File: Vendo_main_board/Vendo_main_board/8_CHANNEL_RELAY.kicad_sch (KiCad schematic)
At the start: 75 parts, among them J10 Conn_01x03_Pin, J11 Conn_01x03_Pin, J12 Conn_01x03_Pin, J5 Conn_01x03_Pin, J6 Conn_01x03_Pin, J7 Conn_01x03_Pin, J8 Conn_01x03_Pin, J9 Conn_01x03_Pin, K1 SRD-05VDC-SL-C, K2 SRD-05VDC-SL-C, K3 SRD-05VDC-SL-C, K4 SRD-05VDC-SL-C, K5 SRD-05VDC-SL-C, K6 SRD-05VDC-SL-C, K7 SRD-05VDC-SL-C, K8 SRD-05VDC-SL-C, Q1 Q_NMOS_Depletion_GSD, Q2 Q_NMOS_Depletion_GSD, Q3 Q_NMOS_Depletion_GSD, Q4 Q_NMOS_Depletion_GSD, Q5 Q_NMOS_Depletion_GSD, Q6 Q_NMOS_Depletion_GSD, Q7 Q_NMOS_Depletion_GSD, Q8 Q_NMOS_Depletion_GSD, U10 PC817, U11 74HC595, U13 PC817, U14 PC817, U15 PC817, U16 PC817, U7 PC817, U8 PC817, U9 PC817

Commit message: -
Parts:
- added J13, J30, J31, J32, J33, J34, J35, J36: Conn_01x02_Pin, symbol Connector:Conn_01x02_Pin
- added J22, J23, J24, J25, J26, J27, J28, J29: Conn_01x03_Pin, symbol Connector:Conn_01x03_Pin
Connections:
- net DC_IN_1_A: now also J13.1 (Pin_1)
- net DC_IN_2_A: now also J30.1 (Pin_1)
- net DC_IN_3_A: now also J31.1 (Pin_1)
- net DC_IN_4_B: now also J32.1 (Pin_1)
- net DC_IN_5_A: now also J36.1 (Pin_1)
- net DC_IN_6_A: now also J35.1 (Pin_1)
- net DC_IN_7_A: now also J34.1 (Pin_1)
- net DC_IN_8_A: now also J33.1 (Pin_1)
- net GNDPWR: now also J13.2 (Pin_2), J30.2 (Pin_2), J31.2 (Pin_2), J32.2 (Pin_2), J33.2 (Pin_2), J34.2 (Pin_2), J35.2 (Pin_2), J36.2 (Pin_2)
- net at J6.1 (Pin_1), K2.3: now also J6.3 (Pin_3), K2.4, J23.2 (Pin_2)
- net at J11.3 (Pin_3), K6.3: now also J11.1 (Pin_1), K6.4, J27.2 (Pin_2)
- net at J12.1 (Pin_1), K5.4: now also J12.3 (Pin_3), K5.3, J26.2 (Pin_2)
- net at J8.1 (Pin_1), K4.3: now also J8.3 (Pin_3), K4.4, J25.2 (Pin_2)
- net at J5.1 (Pin_1), K1.3: now also J5.3 (Pin_3), K1.4, J22.2 (Pin_2)
- net at J10.3 (Pin_3), K7.3: now also J10.1 (Pin_1), K7.4, J29.2 (Pin_2)
- net at J7.1 (Pin_1), K3.3: now also J7.3 (Pin_3), K3.4, J24.2 (Pin_2)
- net at J9.3 (Pin_3), K8.3: now also J9.1 (Pin_1), K8.4, J28.2 (Pin_2)
- new net VIN+_NON_ISO: J22.3 (Pin_3), J23.3 (Pin_3), J24.3 (Pin_3), J25.3 (Pin_3), J26.3 (Pin_3), J27.3 (Pin_3), J28.3 (Pin_3), J29.3 (Pin_3)
- new net VIN+_REL_IN: J22.1 (Pin_1), J23.1 (Pin_1), J24.1 (Pin_1), J25.1 (Pin_1), J26.1 (Pin_1), J27.1 (Pin_1), J28.1 (Pin_1), J29.1 (Pin_1)
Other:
- moved on the sheet: D10, D11, D12, D13, J10, J11, J12, J9, K5, K6, K7, K8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

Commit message: -
added load switch for 12V of coin slot
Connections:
- net SHIT_REG2: now reaches U11.9 (QH')
- no-connect marks 1 -> 0
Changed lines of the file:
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@@
 		(color 0 0 0 0)
 	)
-	(no_connect
-		(at 51.6107 76.2403)
-	)
 	(wire
 		(pts
@@
 		)
 	)
+	(hierarchical_label "SHIT_REG2"
+		(shape input)
+		(at 51.6107 76.2403 0)
+		(effects
+			(font
+				(size 1.27 1.27)
+			)
+			(justify left)
+		)
+	)

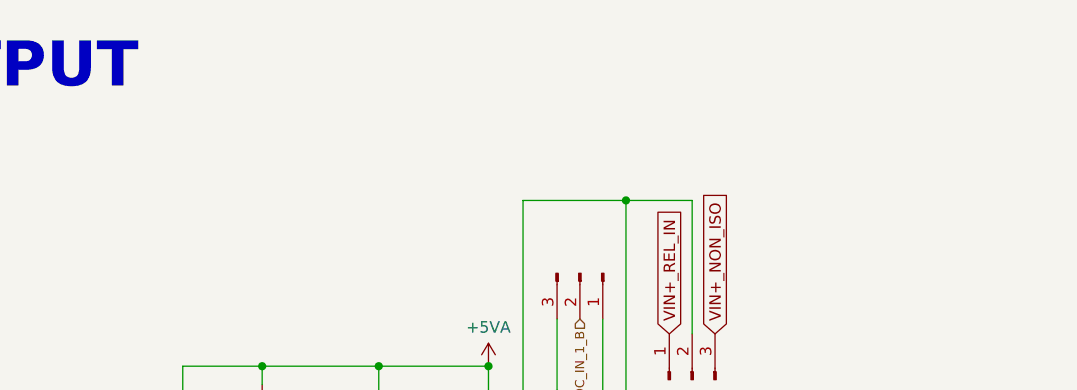
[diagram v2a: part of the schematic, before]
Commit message: -update schematic
-recheck lcsc part number ,value
-check and update footprint assignment
-add load switch for the wdt and ldo combination

-add link for quick connect footprint must be discuss for clarification
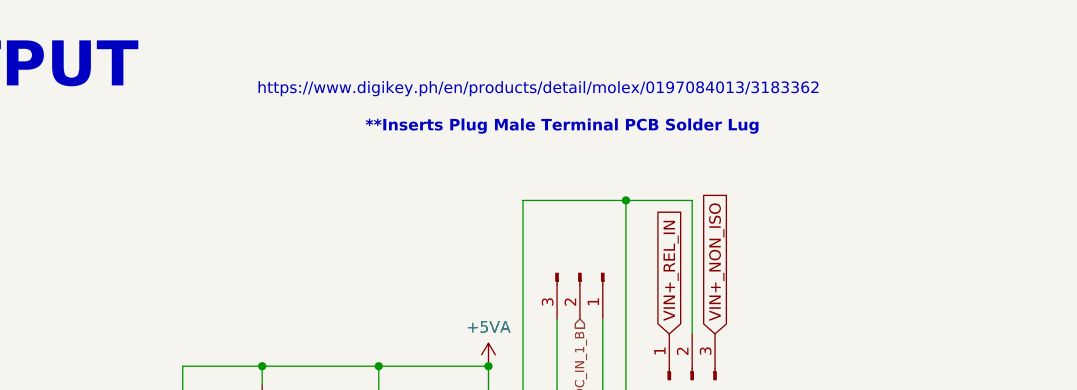
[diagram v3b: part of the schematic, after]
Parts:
- R17, R18, R19, R20, R37, R38, R39, R40: footprint Resistor_SMD:R_0603_1608Metric_Pad0.98x0.95mm_HandSolder -> Resistor_SMD:R_0805_2012Metric_Pad1.20x1.40mm_HandSolder; LCSC C25210 -> C137786
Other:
- note added: "**Inserts Plug Male Terminal PCB Solder Lug"
- note added: "https://www.digikey.ph/en/products/detail/molex/0197084013/3183362"
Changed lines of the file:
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@@
 	(generator_version "9.0")
 	(paper "A3")
+	(text "https://www.digikey.ph/en/products/detail/molex/0197084013/3183362"
+		(exclude_from_sim no)
+		(at 186.1233 23.83 0)
+		(effects
+			(font
+				(size 1.27 1.27)
+			)
+		)
+	)
 	(text "RELAY6\n"
 		(exclude_from_sim no)
@@
 		)
 	)
+	(text "**Inserts Plug Male Terminal PCB Solder Lug"
+		(exclude_from_sim no)
+		(at 188.7905 27.979 0)
+		(effects
+			(font
+				(size 1.27 1.27)
+				(thickness 0.254)
+				(bold yes)
+			)
+		)
+	)
 	(junction
 		(at 193.36 105.1067)
@@
 			)
 		)
-		(property "Footprint" "Resistor_SMD:R_0603_1608Metric_Pad0.98x0.95mm_HandSolder"
+		(property "Footprint" "Resistor_SMD:R_0805_2012Metric_Pad1.20x1.40mm_HandSolder"
 			(at 347.5627 180.4197 90)
 			(effects
@@
 			)
 		)
-		(property "LCSC" "C25210"
+		(property "LCSC" "C137786"
 			(at 347.5627 178.6417 0)
 			(effects
@@
 			)
 		)
-		(property "Footprint" "Resistor_SMD:R_0603_1608Metric_Pad0.98x0.95mm_HandSolder"
+		(property "Footprint" "Resistor_SMD:R_0805_2012Metric_Pad1.20x1.40mm_HandSolder"
 			(at 120.97 130.7607 90)
 			(effects
@@
 			)
 		)
-		(property "LCSC" "C25210"
+		(property "LCSC" "C137786"
 			(at 120.97 128.9827 0)
 			(effects
@@
 			)
 		)
-		(property "Footprint" "Resistor_SMD:R_0603_1608Metric_Pad0.98x0.95mm_HandSolder"
+		(property "Footprint" "Resistor_SMD:R_0805_2012Metric_Pad1.20x1.40mm_HandSolder"
 			(at 120.8622 83.4776 90)
 			(effects
@@
 			)
 		)
-		(property "LCSC" "C25210"
+		(property "LCSC" "C137786"
 			(at 120.8622 81.6996 0)
 			(effects
@@
 			)
 		)
-		(property "Footprint" "Resistor_SMD:R_0603_1608Metric_Pad0.98x0.95mm_HandSolder"
+		(property "Footprint" "Resistor_SMD:R_0805_2012Metric_Pad1.20x1.40mm_HandSolder"
 			(at 347.9876 83.4776 90)
 			(effects
@@
 			)
 		)
-		(property "LCSC" "C25210"
+		(property "LCSC" "C137786"
 			(at 347.9876 81.6996 0)
 			(effects
@@
 			)
 		)
-		(property "Footprint" "Resistor_SMD:R_0603_1608Metric_Pad0.98x0.95mm_HandSolder"
+		(property "Footprint" "Resistor_SMD:R_0805_2012Metric_Pad1.20x1.40mm_HandSolder"
 			(at 347.4549 227.7028 90)
 			(effects
@@
 			)
 		)
-		(property "LCSC" "C25210"
+		(property "LCSC" "C137786"
 			(at 347.4549 225.9248 0)
 			(effects
@@
 			)
 		)
-		(property "Footprint" "Resistor_SMD:R_0603_1608Metric_Pad0.98x0.95mm_HandSolder"
+		(property "Footprint" "Resistor_SMD:R_0805_2012Metric_Pad1.20x1.40mm_HandSolder"
 			(at 347.8798 130.7607 90)
 			(effects
@@
 			)
 		)
-		(property "LCSC" "C25210"
+		(property "LCSC" "C137786"
 			(at 347.8798 128.9827 0)
 			(effects
@@
 			)
 		)
-		(property "Footprint" "Resistor_SMD:R_0603_1608Metric_Pad0.98x0.95mm_HandSolder"
+		(property "Footprint" "Resistor_SMD:R_0805_2012Metric_Pad1.20x1.40mm_HandSolder"
 			(at 121.2871 180.4197 90)
 			(effects
@@
 			)
 		)
-		(property "LCSC" "C25210"
+		(property "LCSC" "C137786"
 			(at 121.2871 178.6417 0)
 			(effects
@@
 			)
 		)
-		(property "Footprint" "Resistor_SMD:R_0603_1608Metric_Pad0.98x0.95mm_HandSolder"
+		(property "Footprint" "Resistor_SMD:R_0805_2012Metric_Pad1.20x1.40mm_HandSolder"
 			(at 121.3949 227.7028 90)
 			(effects
@@
 			)
 		)
-		(property "LCSC" "C25210"
+		(property "LCSC" "C137786"
 			(at 121.3949 225.9248 0)
 			(effects

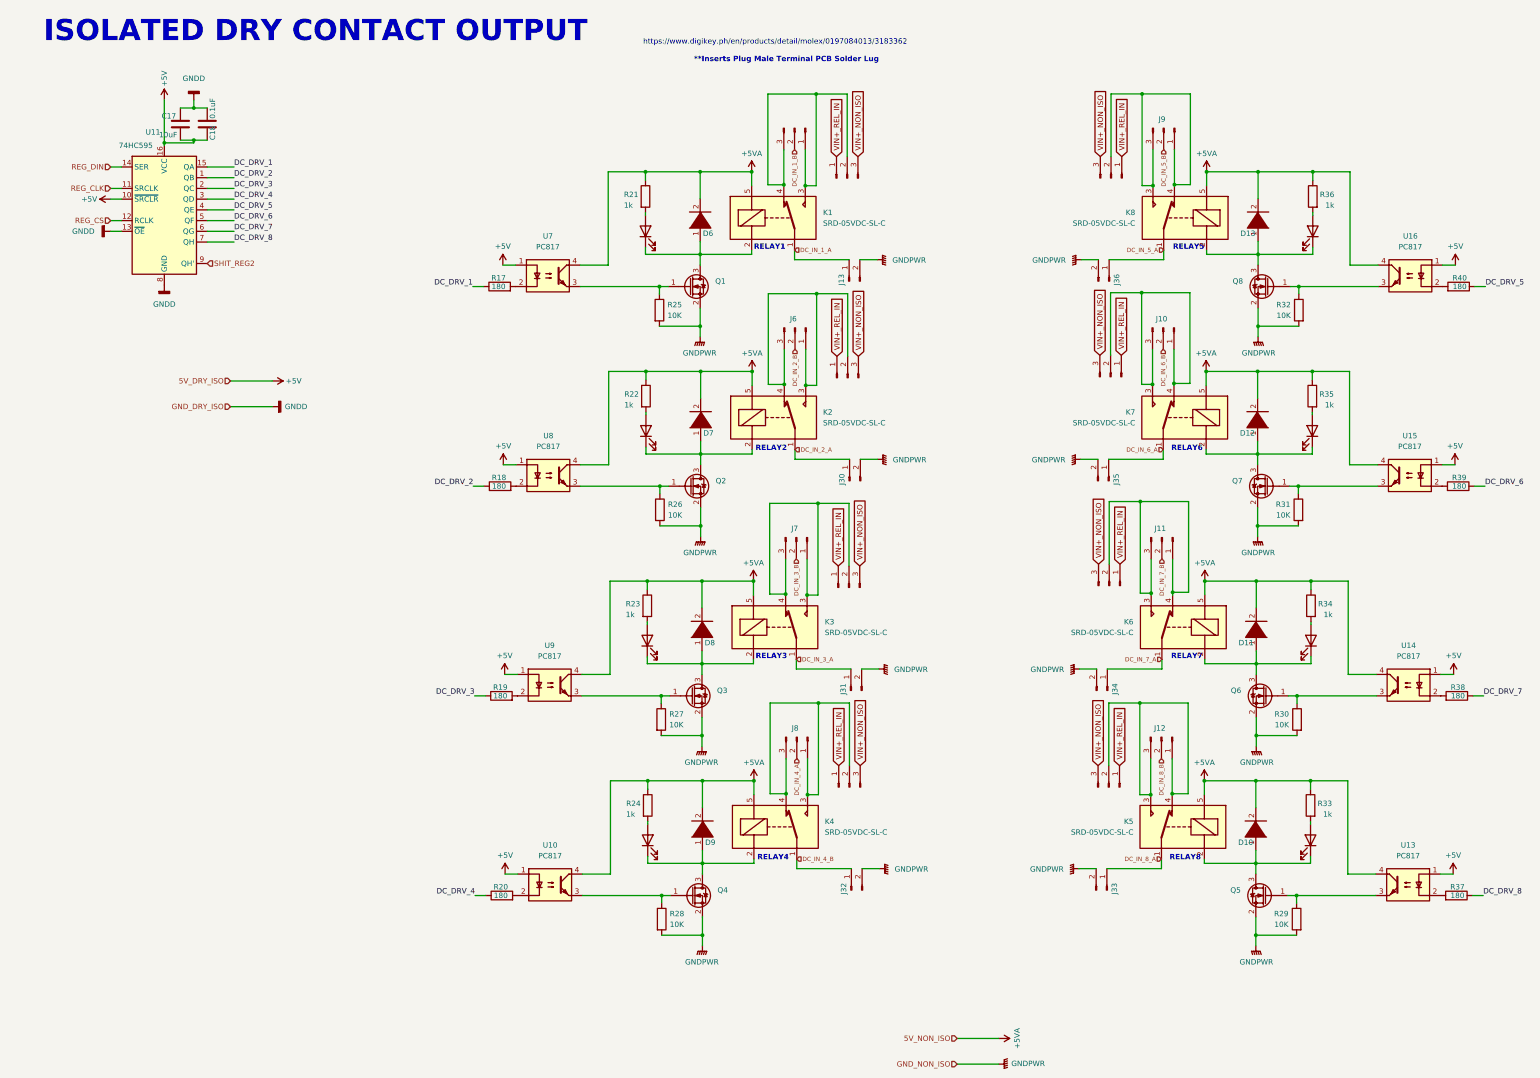
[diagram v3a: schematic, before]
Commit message: -update scheme and pcb placement
update scheme and footprint
added spade connectors
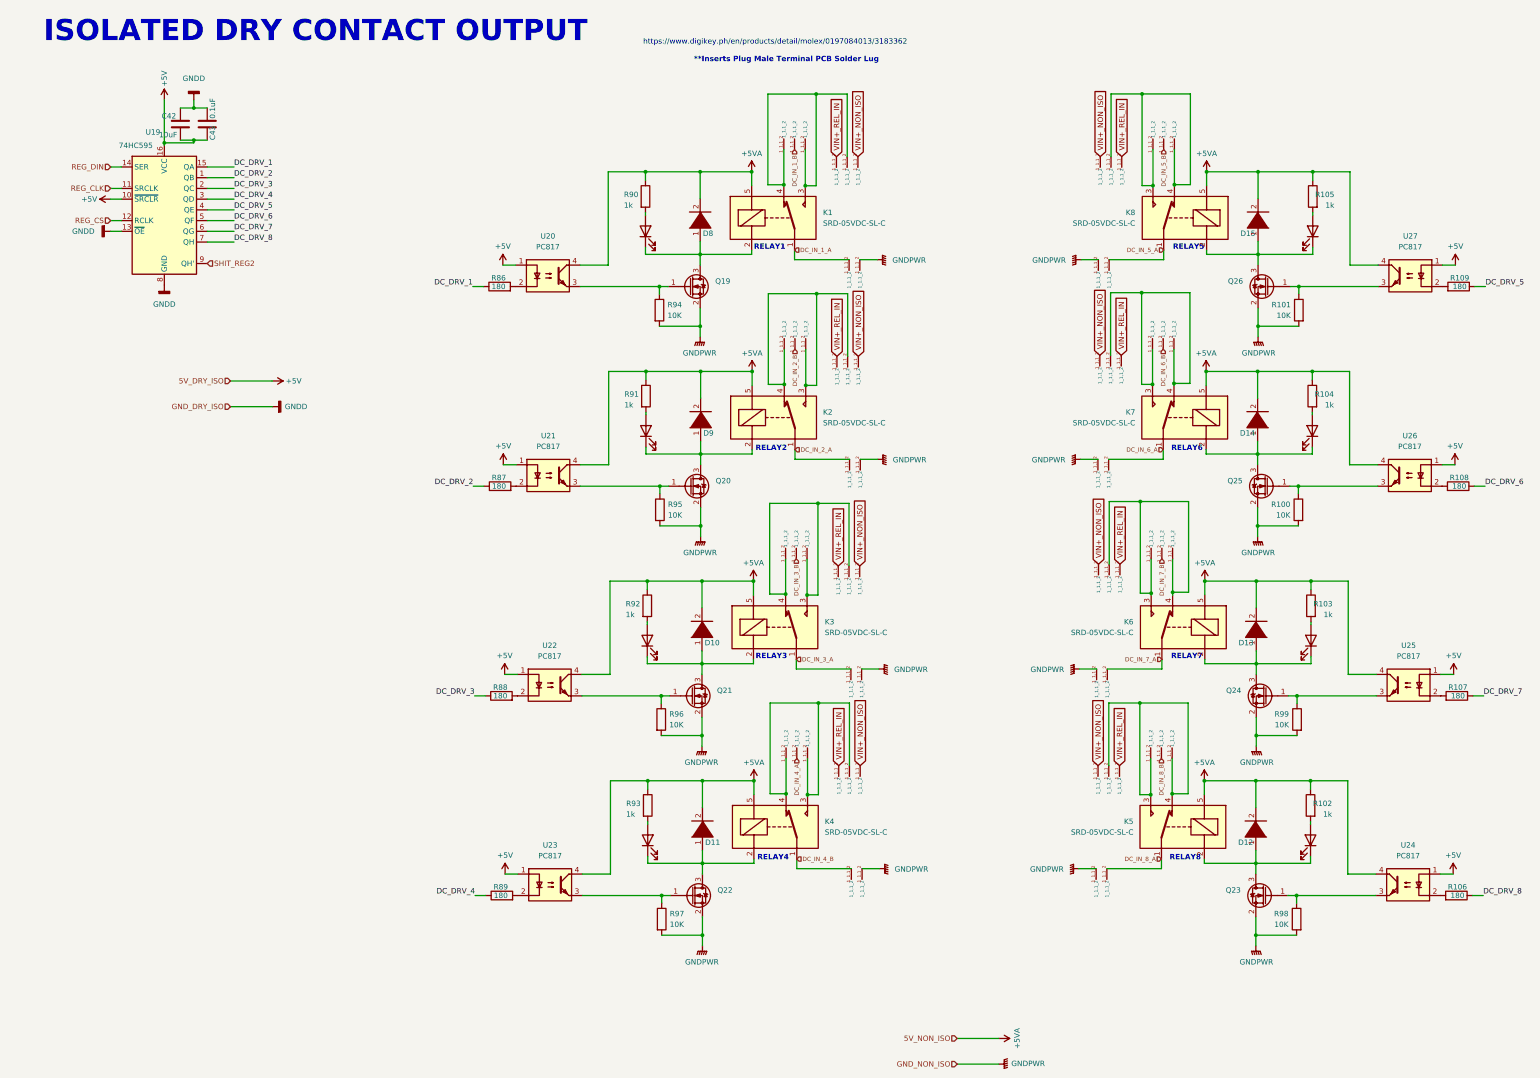
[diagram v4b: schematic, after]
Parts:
- removed J10, J11, J12, J22, J23, J24, J25, J26, J27, J28, J29, J5, J6, J7, J8, J9: Conn_01x03_Pin, symbol Connector:Conn_01x03_Pin
- removed J13, J30, J31, J32, J33, J34, J35, J36: Conn_01x02_Pin, symbol Connector:Conn_01x02_Pin
- added J13, J14, J15, J16, J17, J18, J19, J20, J21, J22, J23, J24, J25, J26, J27, J28, J29, J30, J31, J32, J33, J34, J35, J36, J37, J38, J39, J40, J41, J42, J43, J44, J45, J46, J47, J48, J49, J50, J51, J52, J53, J54, J55, J56, J57, J58, J59, J60, J61, J62, J63, J64, J65, J66, J67, J68, J69, J70, J71, J72, J73, J74, J75, J76: 197084013, InnovKits:Spade Conn4.8mm, symbol Vendo_symbol:197084013
- renumbered C17 to C42, C18 to C43, D8 to D10, D9 to D11, D10 to D12, D11 to D13, D12 to D14, D13 to D15, D14 to D16, D15 to D17, D16 to D18, D17 to D19, D2 to D4, D3 to D5, D4 to D6, D5 to D7, D6 to D8, D7 to D9, Q1 to Q19, Q2 to Q20, Q3 to Q21, Q4 to Q22, Q5 to Q23, Q6 to Q24, Q7 to Q25, Q8 to Q26, R31 to R100, R32 to R101, R33 to R102, R34 to R103, R35 to R104, R36 to R105, R37 to R106, R38 to R107, R39 to R108, R40 to R109, R17 to R86, R18 to R87, R19 to R88, R20 to R89, R21 to R90, R22 to R91, R23 to R92, R24 to R93, R25 to R94, R26 to R95, R27 to R96, R28 to R97, R29 to R98, R30 to R99, U11 to U19, U7 to U20, U8 to U21, U9 to U22, U10 to U23, U13 to U24, U14 to U25, U15 to U26, U16 to U27
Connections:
- net DC_IN_1_A: now also J32.1_1,1_2
- net DC_IN_1_B: now also J17.1_1,1_2
- net DC_IN_2_A: now also J34.1_1,1_2
- net DC_IN_2_B: now also J18.1_1,1_2
- net DC_IN_3_A: now also J35.1_1,1_2
- net DC_IN_3_B: now also J19.1_1,1_2
- net DC_IN_4_A: now also J20.1_1,1_2
- net DC_IN_4_B: now also J36.1_1,1_2
- net DC_IN_5_A: now also J67.1_1,1_2
- net DC_IN_5_B: now also J58.1_1,1_2
- net DC_IN_6_A: now also J65.1_1,1_2
- net DC_IN_6_B: now also J57.1_1,1_2
- net DC_IN_7_A: now also J62.1_1,1_2
- net DC_IN_7_B: now also J52.1_1,1_2
- net DC_IN_8_A: now also J61.1_1,1_2
- net DC_IN_8_B: now also J51.1_1,1_2
- net GNDPWR: now also J40.1_1,1_2, J42.1_1,1_2, J43.1_1,1_2, J44.1_1,1_2, J49.1_1,1_2, J50.1_1,1_2, J53.1_1,1_2, J55.1_1,1_2
- net VIN+_NON_ISO: now also J37.1_1,1_2, J38.1_1,1_2, J39.1_1,1_2, J41.1_1,1_2, J54.1_1,1_2, J56.1_1,1_2, J59.1_1,1_2, J60.1_1,1_2
- net VIN+_REL_IN: now also J25.1_1,1_2, J26.1_1,1_2, J27.1_1,1_2, J28.1_1,1_2, J73.1_1,1_2, J74.1_1,1_2, J75.1_1,1_2, J76.1_1,1_2
- net at K1.3, K1.4: now also J13.1_1,1_2, J21.1_1,1_2, J29.1_1,1_2
- net at K2.3, K2.4: now also J14.1_1,1_2, J22.1_1,1_2, J30.1_1,1_2
- net at K6.3, K6.4: now also J46.1_1,1_2, J64.1_1,1_2, J68.1_1,1_2
- net at K5.3, K5.4: now also J45.1_1,1_2, J63.1_1,1_2, J66.1_1,1_2
- net at K4.3, K4.4: now also J16.1_1,1_2, J24.1_1,1_2, J33.1_1,1_2
- net at K3.3, K3.4: now also J15.1_1,1_2, J23.1_1,1_2, J31.1_1,1_2
- net at K7.3, K7.4: now also J47.1_1,1_2, J69.1_1,1_2, J71.1_1,1_2
- net at K8.3, K8.4: now also J48.1_1,1_2, J70.1_1,1_2, J72.1_1,1_2
